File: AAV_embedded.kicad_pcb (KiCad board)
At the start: 4 copper layers, 168.2 x 114.7 mm, 94 parts, among them J1 JTAG_SWD_CONN, J10 DRV_HIGH_C2, J11 DRV_LOW_C2, J12 DRV_HIGH_C3, J13 DRV_LOW_C3, J14 DRV_LOW_C1, J15 Brake/FwRev, J16 5v_in, J17 3.3v_in, J18 12v_in, J2 Raspberry_Pi_4, J21 CAN, J23 5v_rail, J24 3.3v_rail, J25 12v_rail, J26 GND_rail, J27 12v_rail_f, J28 3.3v_rail_f, J29 5v_rail_f, J3 USB_C_Receptacle_USB2.0_14P, J30 GND_rail_f, J32 Conn_02x15_Counter_Clockwise, J34 Conn_02x15_Counter_Clockwise, J5 THR_EN_JMP, J6 Conn_01x07, J7 Conn_01x05, J8 Throttle Connector, J9 DRV_HIGH_C1, SW10 SW_DIP_x02, SW2 IO_EXT_ADDR, SW4 5v_USB_EN, SW5 THR_EN, SW6 ~{RESET_uMOD}, SW7 ~{BOOT_uMOD}, SW8 ~{RESET_BRK}, SW9 ~{RESET_STR}, U1 DAC101C081CIMK, U2 PCA9555D, U3 74AHC1G08, U5 FXMA108, U6 MCP2515-xSO, U7 SN65HVD230, Y1 16MHz

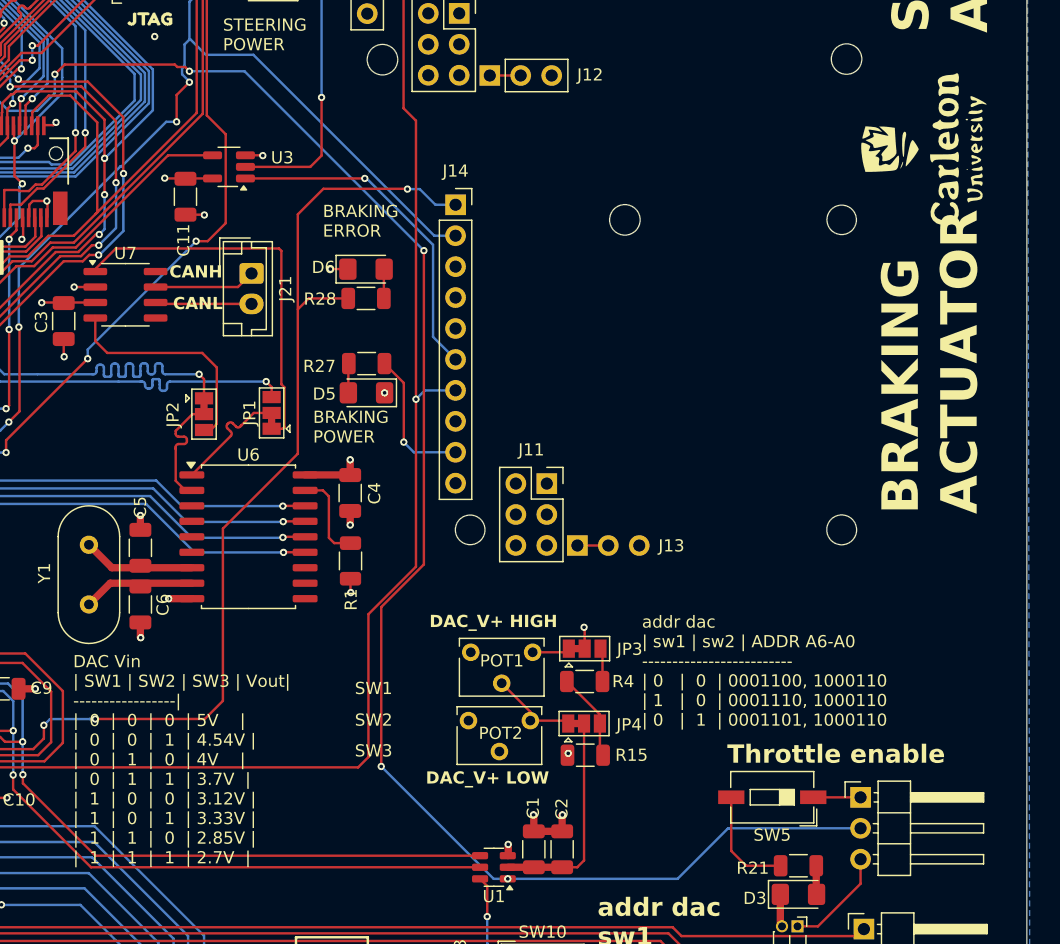
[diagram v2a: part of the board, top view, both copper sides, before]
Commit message: remove dip switch table silkscreen
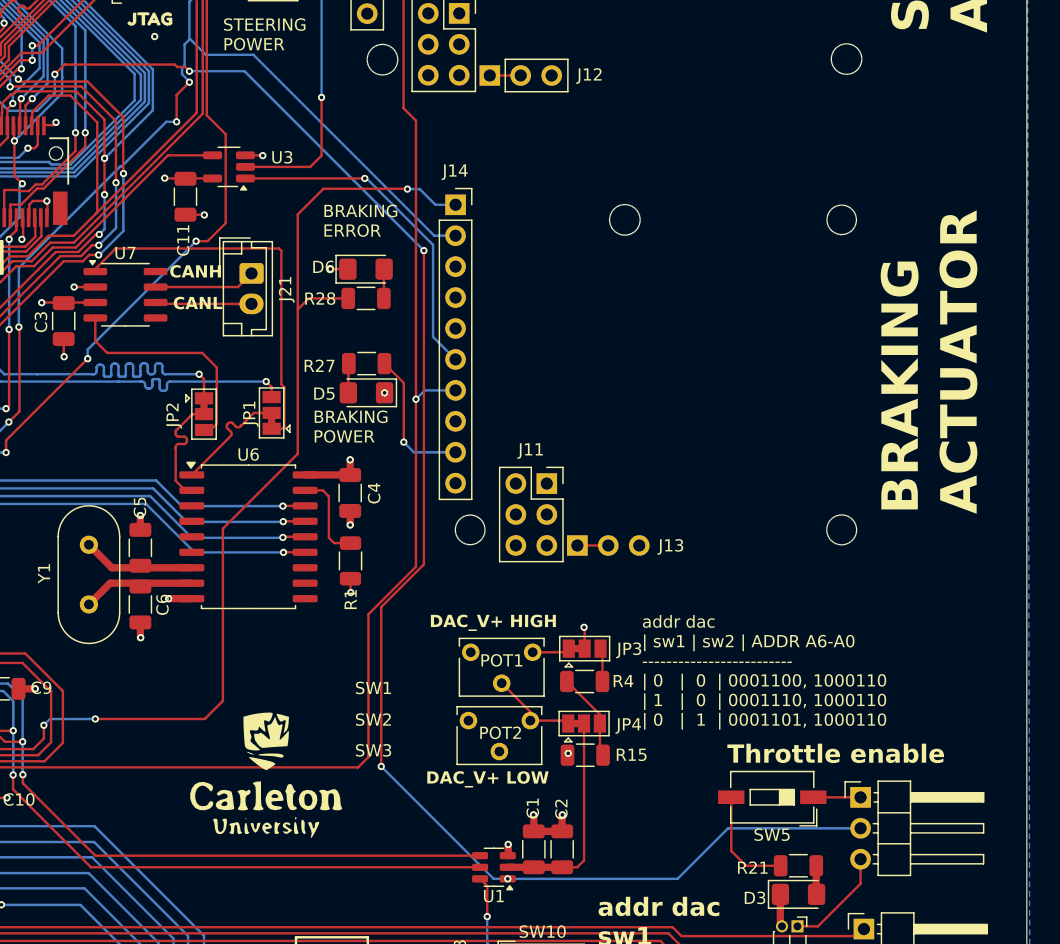
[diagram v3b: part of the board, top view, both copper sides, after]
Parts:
- moved G*** 74.6 mm to (153.8, 136.2), turned to 0 degrees
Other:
- board text removed: "DAC Vin | SW1 | SW2 | SW3 | Vout| -----------------| | 0 | 0 | 0 | 5V | | 0 | 0 | 1 | 4.54V | | 0 | 1 | 0 | 4V | | 0 | 1 | 1 | 3.7V | | 1 | 0 | 0 | 3.12V | | 1 | 0 | 1 | 3.33V | | 1 | 1 | 0 | 2.85V | | 1 | 1 | 1 | 2.7V |"
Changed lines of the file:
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@@
 	(footprint "LOGO"
 		(layer "F.Cu")
-		(at 207.75 84.8 90)
+		(at 153.75 136.2)
 		(property "Reference" "G***"
-			(at 0 0 90)
+			(at 0 0 360)
 			(layer "F.SilkS")
 			(hide yes)
@@
 		)
 		(property "Value" "LOGO"
-			(at 0.75 0 90)
+			(at 0.75 0 360)
 			(layer "F.SilkS")
 			(hide yes)
@@
 		)
 		(property "Footprint" ""
-			(at 0 0 90)
+			(at 0 0 360)
 			(layer "F.Fab")
 			(hide yes)
@@
 		)
 		(property "Datasheet" ""
-			(at 0 0 90)
+			(at 0 0 360)
 			(layer "F.Fab")
 			(hide yes)
@@
 		)
 		(property "Description" ""
-			(at 0 0 90)
+			(at 0 0 360)
 			(layer "F.Fab")
 			(hide yes)
@@
 		(fp_poly
 			(pts
-				(xy 0.961136 -5.04219) (xy 1.164971 -4.997021) (xy 1.390223 -4.936802) (xy 1.880936 -4.797207) (xy 1.844994 -4.300315)
-				(xy 1.801352 -3.965446) (xy 1.717384 -3.74382) (xy 1.613915 -3.616211) (xy 1.418777 -3.429) (xy 1.46734 -3.640666)
-				(xy 1.511774 -3.860446) (xy 1.562097 -4.144717) (xy 1.574639 -4.221757) (xy 1.605601 -4.446552)
-				(xy 1.592755 -4.538043) (xy 1.52184 -4.529665) (xy 1.457254 -4.496924) (xy 1.28244 -4.422122) (xy 1.192036 -4.402666)
-				(xy 1.115874 -4.470588) (xy 1.015869 -4.632457) (xy 0.923147 -4.825425) (xy 0.868838 -4.986648)
-				(xy 0.871977 -5.048865)
+				(xy -0.498465 3.902273) (xy -0.468258 3.951882) (xy -0.502447 4.083677) (xy -0.583929 4.296834)
+				(xy -0.723491 4.586033) (xy -0.852899 4.707505) (xy -0.977627 4.662133) (xy -1.103149 4.4508) (xy -1.130297 4.384972)
+				(xy -1.218216 4.159638) (xy -1.276117 4.008405) (xy -1.286649 3.979334) (xy -1.229988 3.930047)
+				(xy -1.158146 3.909625) (xy -1.039745 3.945878) (xy -1.016 4.050867) (xy -0.98904 4.273371) (xy -0.922229 4.418029)
+				(xy -0.837795 4.439517) (xy -0.78328 4.329385) (xy -0.762 4.14367) (xy -0.733986 3.959744) (xy -0.63103 3.896548)
+				(xy -0.594081 3.894667)
 			)
 			(stroke
@@
 		(fp_poly
 			(pts
-				(xy -0.498465 3.902273) (xy -0.468258 3.951882) (xy -0.502447 4.083677) (xy -0.583929 4.296834)
-				(xy -0.723491 4.586033) (xy -0.852899 4.707505) (xy -0.977627 4.662133) (xy -1.103149 4.4508) (xy -1.130297 4.384972)
-				(xy -1.218216 4.159638) (xy -1.276117 4.008405) (xy -1.286649 3.979334) (xy -1.229988 3.930047)
-				(xy -1.158146 3.909625) (xy -1.039745 3.945878) (xy -1.016 4.050867) (xy -0.98904 4.273371) (xy -0.922229 4.418029)
-				(xy -0.837795 4.439517) (xy -0.78328 4.329385) (xy -0.762 4.14367) (xy -0.733986 3.959744) (xy -0.63103 3.896548)
-				(xy -0.594081 3.894667)
+				(xy 0.961136 -5.04219) (xy 1.164971 -4.997021) (xy 1.390223 -4.936802) (xy 1.880936 -4.797207) (xy 1.844994 -4.300315)
+				(xy 1.801352 -3.965446) (xy 1.717384 -3.74382) (xy 1.613915 -3.616211) (xy 1.418777 -3.429) (xy 1.46734 -3.640666)
+				(xy 1.511774 -3.860446) (xy 1.562097 -4.144717) (xy 1.574639 -4.221757) (xy 1.605601 -4.446552)
+				(xy 1.592755 -4.538043) (xy 1.52184 -4.529665) (xy 1.457254 -4.496924) (xy 1.28244 -4.422122) (xy 1.192036 -4.402666)
+				(xy 1.115874 -4.470588) (xy 1.015869 -4.632457) (xy 0.923147 -4.825425) (xy 0.868838 -4.986648)
+				(xy 0.871977 -5.048865)
 			)
 			(stroke
@@
 		(fp_poly
 			(pts
-				(xy 2.094059 0.753146) (xy 2.185861 0.912584) (xy 2.188394 0.928016) (xy 2.265851 1.132432) (xy 2.357727 1.239469)
-				(xy 2.451907 1.325814) (xy 2.400497 1.379125) (xy 2.3495 1.400012) (xy 2.264966 1.466635) (xy 2.219203 1.609672)
-				(xy 2.202281 1.868576) (xy 2.201333 1.98885) (xy 2.20789 2.284215) (xy 2.236163 2.452315) (xy 2.299055 2.534989)
-				(xy 2.379587 2.566865) (xy 2.505646 2.646239) (xy 2.521224 2.724906) (xy 2.414661 2.818298) (xy 2.224136 2.861503)
-				(xy 2.030944 2.841261) (xy 1.973797 2.81421) (xy 1.838866 2.63969) (xy 1.741745 2.341826) (xy 1.695444 1.964779)
-				(xy 1.693333 1.862152) (xy 1.676515 1.610713) (xy 1.633745 1.435561) (xy 1.604555 1.394459) (xy 1.564653 1.295445)
-				(xy 1.596443 1.241296) (xy 1.670645 1.084186) (xy 1.706387 0.931334) (xy 1.791076 0.762956) (xy 1.941382 0.703415)
+				(xy -1.321269 1.225836) (xy -1.27 1.356762) (xy -1.347407 1.525312) (xy -1.481667 1.608667) (xy -1.61057 1.678985)
+				(xy -1.673337 1.796406) (xy -1.692633 2.013991) (xy -1.693333 2.104204) (xy -1.663973 2.422812)
+				(xy -1.580637 2.611337) (xy -1.567266 2.623893) (xy -1.477579 2.748064) (xy -1.548263 2.833056)
+				(xy -1.774053 2.8749) (xy -1.905 2.878667) (xy -2.141097 2.862966) (xy -2.296838 2.82347) (xy -2.322405 2.803593)
+				(xy -2.305542 2.695813) (xy -2.242735 2.623893) (xy -2.15733 2.46704) (xy -2.1143 2.214028) (xy -2.11252 1.924856)
+				(xy -2.150865 1.659523) (xy -2.228211 1.478027) (xy -2.264833 1.44509) (xy -2.363768 1.365068) (xy -2.314296 1.292498)
+				(xy -2.286 1.272846) (xy -2.064443 1.194801) (xy -1.835097 1.211826) (xy -1.719823 1.277377) (xy -1.617624 1.323633)
+				(xy -1.570893 1.277377) (xy -1.446508 1.187815)
 			)
 			(stroke
@@
 		(fp_poly
 			(pts
-				(xy -1.321269 1.225836) (xy -1.27 1.356762) (xy -1.347407 1.525312) (xy -1.481667 1.608667) (xy -1.61057 1.678985)
-				(xy -1.673337 1.796406) (xy -1.692633 2.013991) (xy -1.693333 2.104204) (xy -1.663973 2.422812)
-				(xy -1.580637 2.611337) (xy -1.567266 2.623893) (xy -1.477579 2.748064) (xy -1.548263 2.833056)
-				(xy -1.774053 2.8749) (xy -1.905 2.878667) (xy -2.141097 2.862966) (xy -2.296838 2.82347) (xy -2.322405 2.803593)
-				(xy -2.305542 2.695813) (xy -2.242735 2.623893) (xy -2.15733 2.46704) (xy -2.1143 2.214028) (xy -2.11252 1.924856)
-				(xy -2.150865 1.659523) (xy -2.228211 1.478027) (xy -2.264833 1.44509) (xy -2.363768 1.365068) (xy -2.314296 1.292498)
-				(xy -2.286 1.272846) (xy -2.064443 1.194801) (xy -1.835097 1.211826) (xy -1.719823 1.277377) (xy -1.617624 1.323633)
-				(xy -1.570893 1.277377) (xy -1.446508 1.187815)
+				(xy 2.094059 0.753146) (xy 2.185861 0.912584) (xy 2.188394 0.928016) (xy 2.265851 1.132432) (xy 2.357727 1.239469)
+				(xy 2.451907 1.325814) (xy 2.400497 1.379125) (xy 2.3495 1.400012) (xy 2.264966 1.466635) (xy 2.219203 1.609672)
+				(xy 2.202281 1.868576) (xy 2.201333 1.98885) (xy 2.20789 2.284215) (xy 2.236163 2.452315) (xy 2.299055 2.534989)
+				(xy 2.379587 2.566865) (xy 2.505646 2.646239) (xy 2.521224 2.724906) (xy 2.414661 2.818298) (xy 2.224136 2.861503)
+				(xy 2.030944 2.841261) (xy 1.973797 2.81421) (xy 1.838866 2.63969) (xy 1.741745 2.341826) (xy 1.695444 1.964779)
+				(xy 1.693333 1.862152) (xy 1.676515 1.610713) (xy 1.633745 1.435561) (xy 1.604555 1.394459) (xy 1.564653 1.295445)
+				(xy 1.596443 1.241296) (xy 1.670645 1.084186) (xy 1.706387 0.931334) (xy 1.791076 0.762956) (xy 1.941382 0.703415)
 			)
 			(stroke
@@
 			)
 			(justify left bottom)
-		)
-	)
-	(gr_text "DAC Vin \n| SW1 | SW2 | SW3 | Vout|\n-----------------|\n|  0  |  0  |  0  | 5V    | \n|  0  |  0  |  1  | 4.54V | \n|  0  |  1  |  0  | 4V    | \n|  0  |  1  |  1  | 3.7V  | \n|  1  |  0  |  0  | 3.12V |\n|  1  |  0  |  1  | 3.33V | \n|  1  |  1  |  0  | 2.85V | \n|  1  |  1  |  1  | 2.7V  |  "
-		(at 137.9 143.55 0)
-		(layer "F.SilkS")
-		(effects
-			(font
-				(size 1 1)
-				(thickness 0.15)
-			)
-			(justify left bottom)

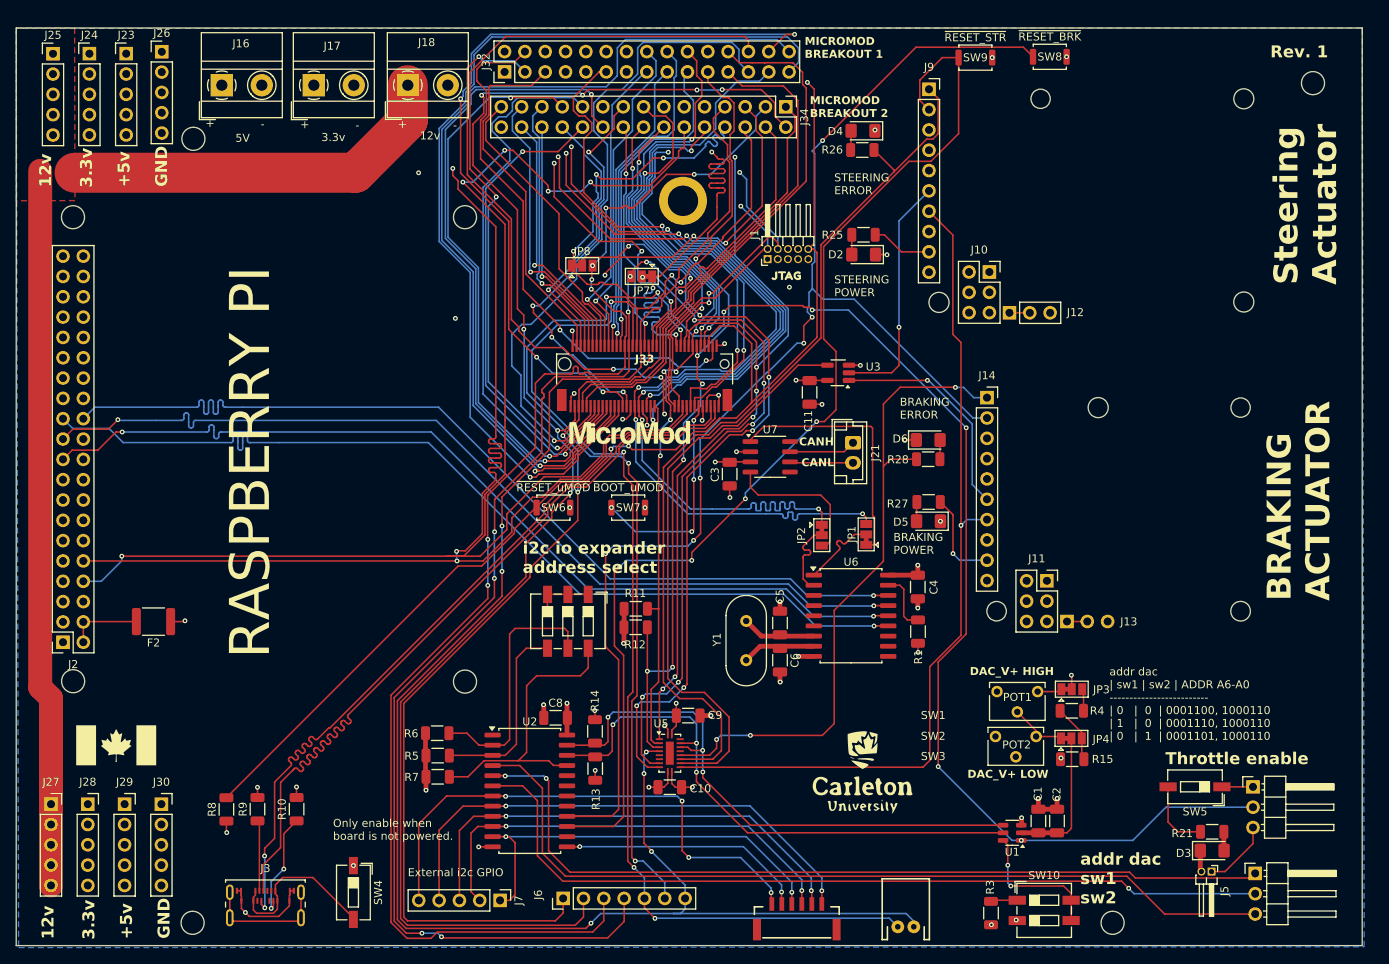
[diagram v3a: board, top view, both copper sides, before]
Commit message: add jlc tracking
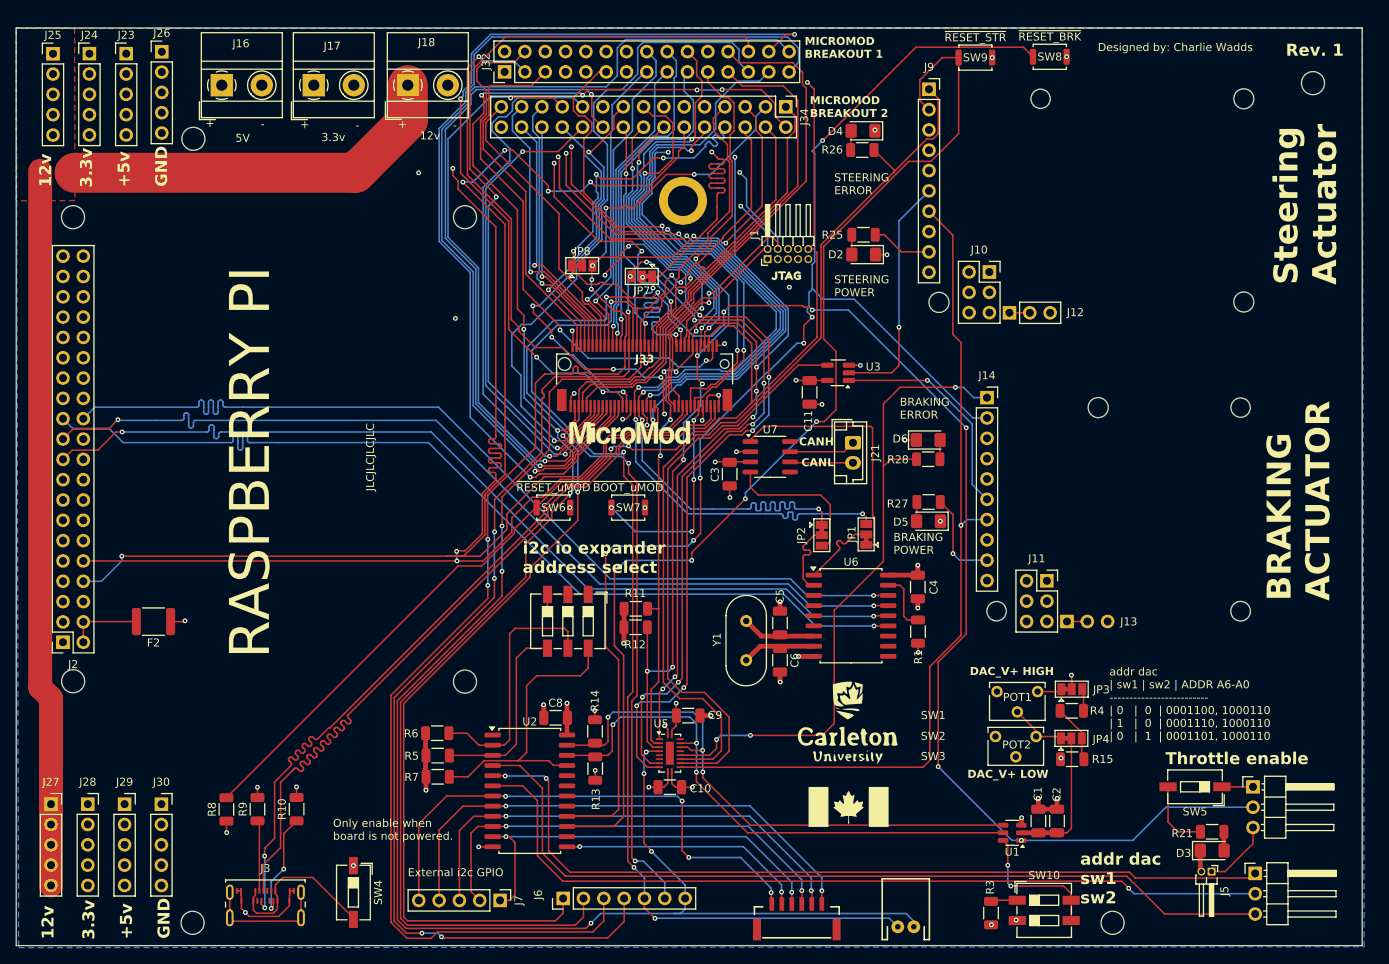
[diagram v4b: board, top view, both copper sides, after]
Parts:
- moved G*** 91.9 mm to (152.0, 140.5)
- moved G*** 6.47 mm to (151.9, 130.0)
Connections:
- J2 pad 1: Net-(J2-3V3-Pad1) -> unconnected-(J2-3V3-Pad1)
- J2 pad 17: Net-(J2-3V3-Pad1) -> unconnected-(J2-3V3-Pad1)_1
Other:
- board text added: "Designed by: Charlie Wadds"
- board text added: "JLCJLCJLCJLC"

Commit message: silkscreen
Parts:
- removed the G*** at (152.0, 140.5)
- added G***1: LOGO, LOGO, F.Cu at (211.8, 45.9)
